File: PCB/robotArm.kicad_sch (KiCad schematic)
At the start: 84 parts, among them J1 Motor_eje_X, J10 Gripper, J11 Conector Auxiliar 2, J12 5v, J13 End-Stop-X, J14 End-Stop-Y, J15 End-Stop-Z, J16 jumperLed5v, J17 Conector Auxiliar 1, J18 Pulsador Externo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

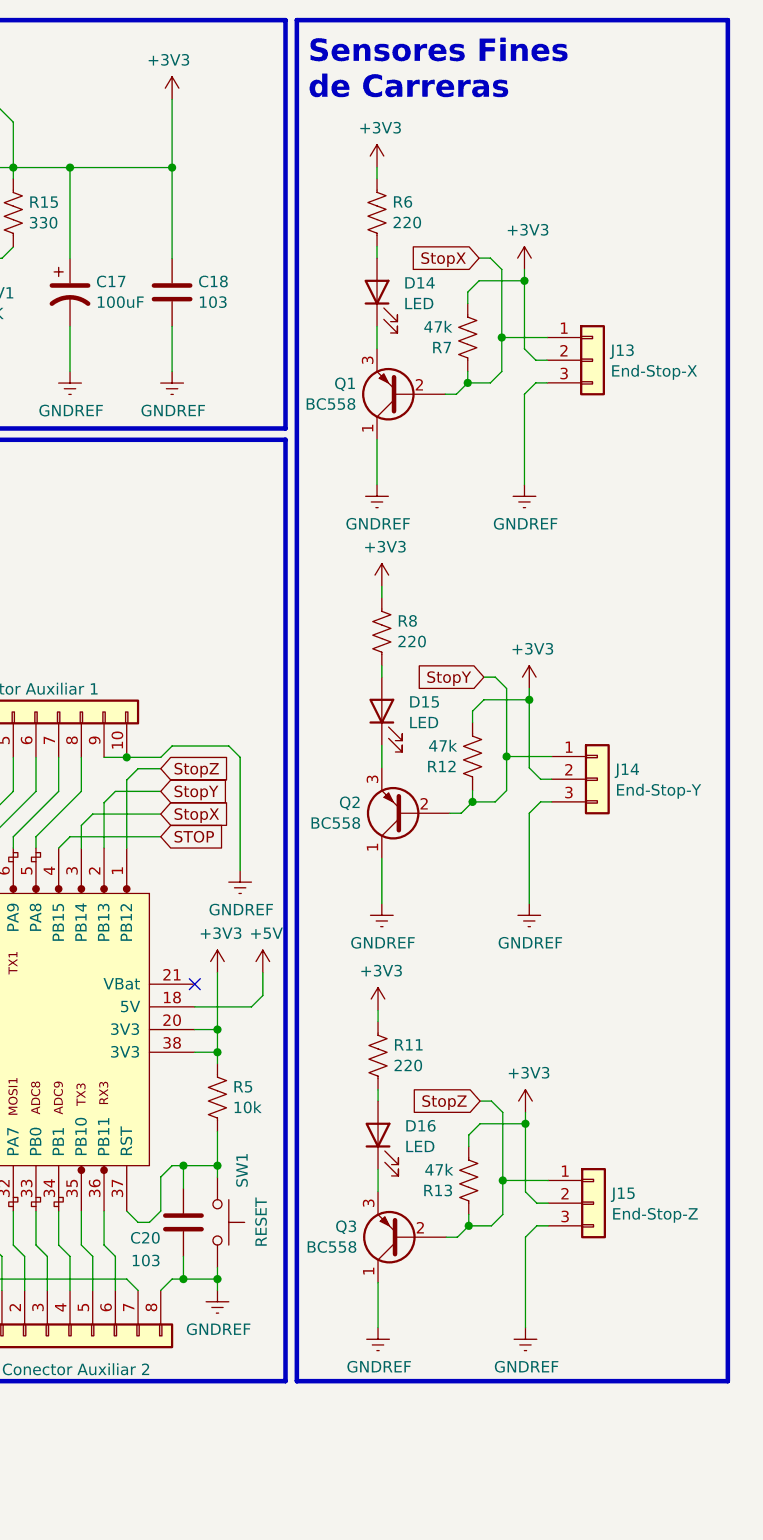
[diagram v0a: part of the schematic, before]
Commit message: Limpieza: Eliminación de archivos temporales de KiCad
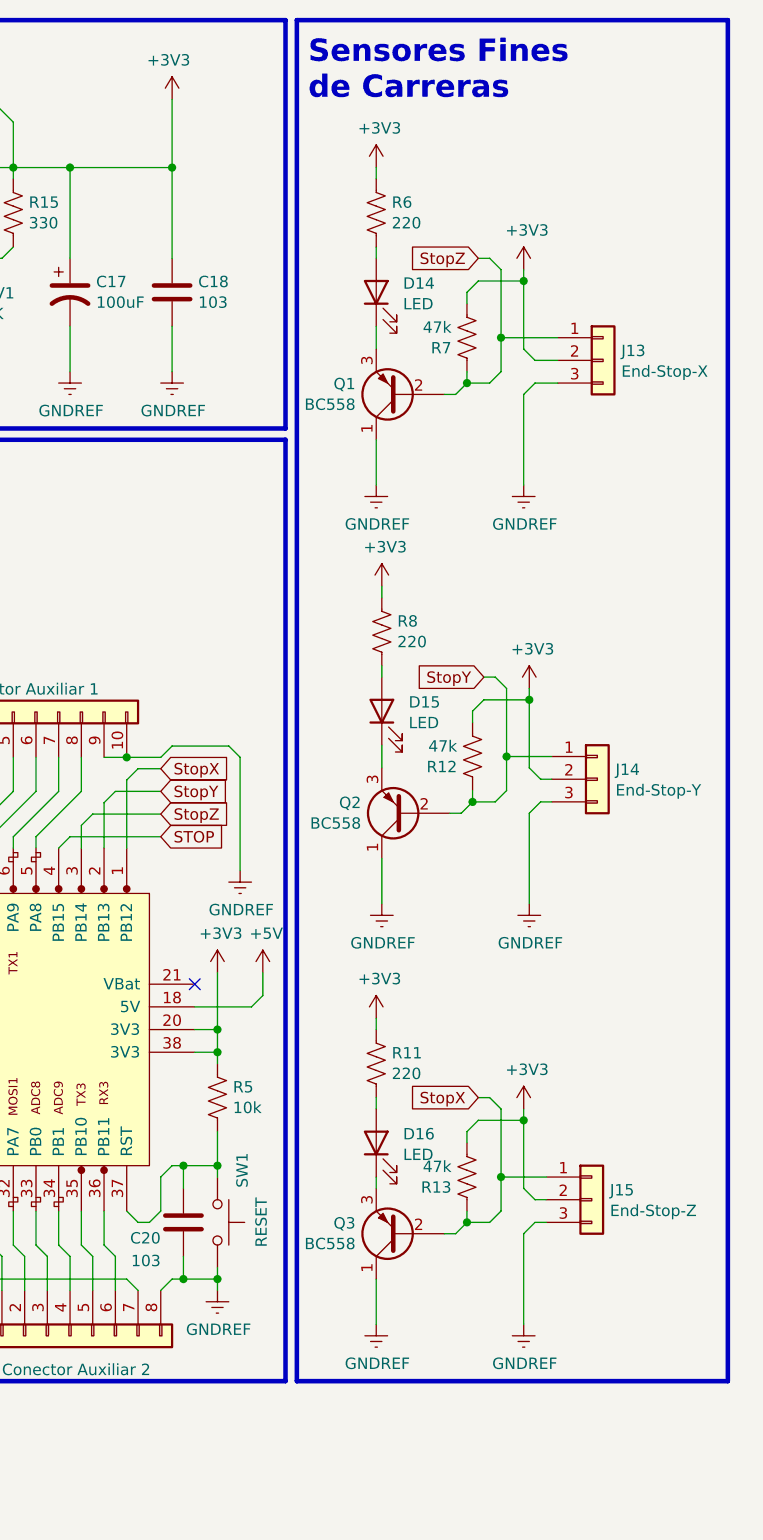
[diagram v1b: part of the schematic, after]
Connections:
- net StopX: now also J15.1 (Pin_1), Q3.2 (B), R13.1, U1.1 (PB12); no longer J13.1 (Pin_1), Q1.2 (B), R7.1, U1.3 (PB14)
- net StopZ: now also J13.1 (Pin_1), Q1.2 (B), R7.1, U1.3 (PB14); no longer J15.1 (Pin_1), Q3.2 (B), R13.1, U1.1 (PB12)
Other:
- moved on the sheet: D16, J13, R11
